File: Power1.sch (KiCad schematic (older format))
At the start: 88 parts, among them J2 XT60PW-M, Q4 BSS138W, Q5 SISS30DN-T1-GE3, Q6 SISS30DN-T1-GE3, U3 LMR33630BRNXR, U4 TPS2121RUXT, U5 BTS6143DAUMA1, U6 LTC3862EUH-1#PBF

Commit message: PVT
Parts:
- removed C15, C17, C20: 22u, Capacitor-Chip:C_CHIP_2012_Reflow, symbol passive:C
- removed C16: 100n, Capacitor-Chip:C_CHIP_1005_Hand_NoSilk, symbol passive:C
- removed R17: 1k, Resistor-Chip:R_CHIP_1005_Hand_NoSilk, symbol passive:R
- added C17: 47u, Phoenix:C_RADIAL_5.0_P2.0_D0.5, symbol passive:CE_Polarity
- added C19, C21, C22, C8: 10u, Capacitor-Chip:C_CHIP_2012_Reflow, symbol passive:C
- added C38, C40: 100n, Capacitor-Chip:C_CHIP_1608_Reflow, symbol passive:C
- C12: renamed from C10; PartName C1005X5R1V105K050BE -> TMK105BJ105MV-F
- C16: renamed from C14; PartName C1005X5R1V105K050BE -> TMK105BJ105MV-F
- C18: value 22u -> 10u; PartName GRM21BR61E226ME44L -> GRM21BC8YA106KE11L
- C20: renamed from C19; PartName UVZ1V331MPD -> 35ZLH330MEFCT810X12.5
- C25: renamed from C23; footprint Capacitor-Chip:C_CHIP_1608_Reflow -> Capacitor-Chip:C_CHIP_2012_Reflow; PartName EMK107BBJ106MA-T -> GRM21BC8YA106KE11L
- C28: renamed from C26; PartName UMK325BJ106MM-P -> GMK325BJ106KN-T
- C29: renamed from C27; footprint Capacitor-Chip:C_CHIP_1608_Reflow -> Capacitor-Chip:C_CHIP_1005_Hand_NoSilk; PartName GRM188R61E105KA12D -> TMK105BJ105MV-F
- C32: renamed from C30; PartName UMK325BJ106MM-P -> GMK325BJ106KN-T
- C33: renamed from C31; PartName UMK325BJ106MM-P -> GMK325BJ106KN-T
- C34: renamed from C33; value 33u -> 56u; PartName 63PZE33M8X9 -> 63SXE56M
- C35: renamed from C32; PartName UMK325BJ106MM-P -> GMK325BJ106KN-T
- C36: value 33u -> 56u; PartName 63PZE33M8X9 -> 63SXE56M
- C37: renamed from C34; PartName UMK325BJ106MM-P -> GMK325BJ106KN-T
- C39: renamed from C35; PartName UMK325BJ106MM-P -> GMK325BJ106KN-T
- C7: renamed from C6; footprint Capacitor-Chip:C_CHIP_3225_Reflow -> Capacitor-Chip:C_CHIP_2012_Reflow; PartName UMK325BJ106MM-P -> GRM21BC8YA106KE11L
- C9: renamed from C8; value 4.7u -> 10u; PartName (none) -> GRM21BC8YA106KE11L
- F1: value 30A -> 25A; PartName 0685H9300-01 -> 0685H9250-01
- R21: renamed from R22; value 68k -> 75k; PartName RK73H1ETTP6802F -> RK73H1ETTP7502F
- R22: renamed from R23; value 30k -> 43k; PartName RK73H1ETTP3002F -> RK73H1ETTP4302F
- R30: renamed from R31; value 5m -> 7m; PartName KRL6432E-M-R005-F-T1 -> KRL6432E-M-R007-F-T1
- R31: renamed from R32; value 5m -> 7m; PartName KRL6432E-M-R005-F-T1 -> KRL6432E-M-R007-F-T1
- U4: value TPS2121RUXT -> TPS2121RUXR; PartName TPS2121RUXT -> TPS2121RUXR
- renumbered C7 to C10, C9 to C11, C11 to C13, C12 to C14, C13 to C15, C21 to C23, C22 to C24, C24 to C26, C25 to C27, C28 to C30, C29 to C31, R14 to R13, R13 to R14, R20 to R17, R21 to R18, R18 to R19, R19 to R20, R24 to R23, R25 to R24, R26 to R25, R27 to R26, R28 to R27, R29 to R28, R30 to R29
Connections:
- net +12V: now also U4.7 (IN1), C19.1, C21.1, C22.1; no longer U4.2 (IN2)
- net +48V: now also C38.1, C40.1
- net GND: now also U4.3 (CP2), U4.5 (OV1), C17.2, C19.2, C21.2, C22.2, C38.2, C40.2, C8.2; no longer U4.4 (OV2), U4.6 (PR1)
- net VBAT: now also C8.1
- net VBUS: now also U4.2 (IN2); no longer U4.7 (IN1)
- net VSYS: now also C17.1
- net at U5.2 (IN): now also Q4.3 (D)
- net at R13.1, R15.2: now also U4.6 (PR1); no longer U4.3 (CP2)
- net at R12.1, R14.2: now also U4.4 (OV2); no longer U4.5 (OV1)
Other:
- note added: "VBAT to 48V/8A Boost Converter"
- note added: "old\nST=Z : IN1(VBUS) is selected\nST=L : IN2(12V) is selected"
- note removed: "ST=Z : IN1(VBUS) is selected\nST=L : IN2(12V) is selected"
- note removed: "VBAT to 48V/10A Boost Converter"
- moved on the sheet: C10, C11, C12, C15, C34, C36, C9, L1, R12, R13, R14, R15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

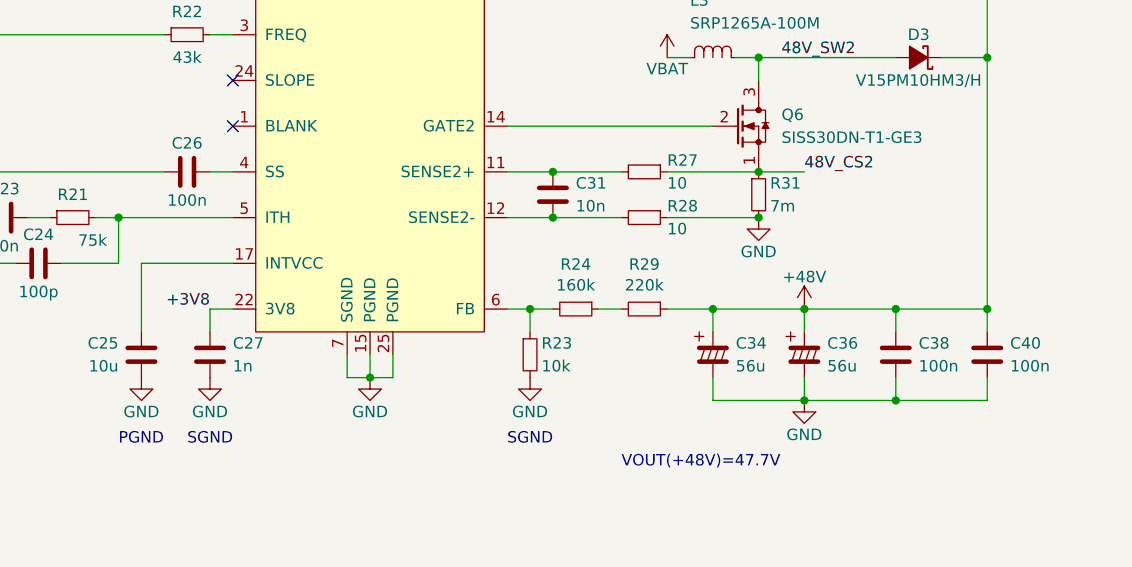
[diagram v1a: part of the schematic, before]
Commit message: SBUにTVSダイオードを追加
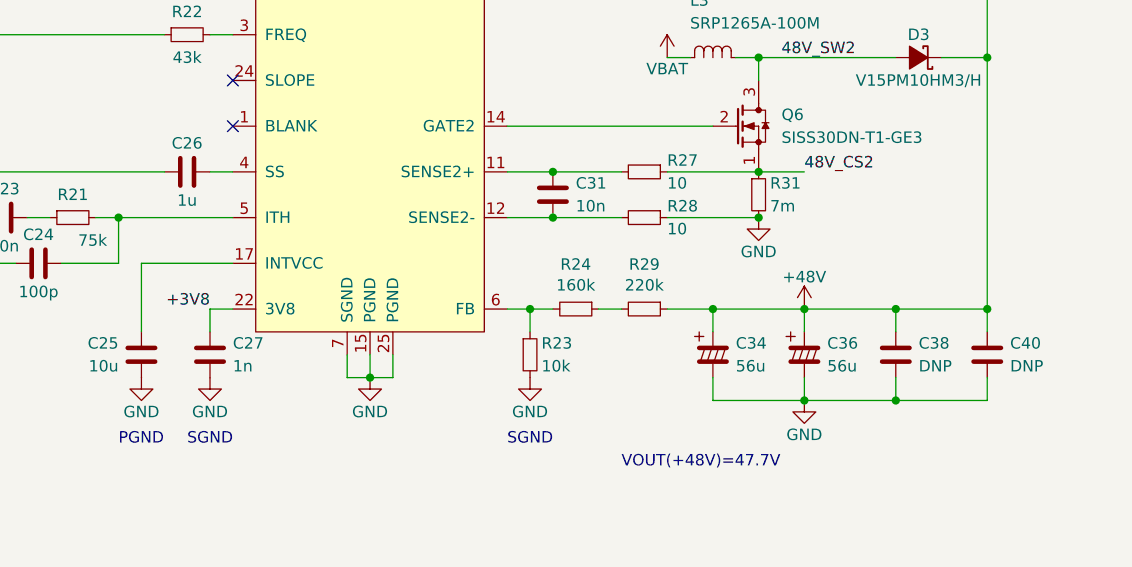
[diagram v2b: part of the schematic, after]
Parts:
- C26: value 100n -> 1u; PartName GRM155R71H104ME14D -> TMK105BJ105MV-F
- C38, C40: value 100n -> DNP; Supplier (none) -> None
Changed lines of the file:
@@
 P 7200 5100
 F 0 "C26" V 7075 5100 50  0000 C CNN
-F 1 "100n" V 7325 5100 50  0000 C CNN
+F 1 "1u" V 7325 5100 50  0000 C CNN
 F 2 "Capacitor-Chip:C_CHIP_1005_Hand_NoSilk" H 7300 5000 50  0001 C CNN
 F 3 "" H 7225 5200 50  0001 C CNN
-F 4 "GRM155R71H104ME14D" H 7200 5100 50  0001 C CNN "PartName"
+F 4 "TMK105BJ105MV-F" H 7200 5100 50  0001 C CNN "PartName"
 	1    7200 5100
 	0    -1   1    0
@@
 AR Path="/5E314B49/5FB00ABF" Ref="C38"  Part="1"
 F 0 "C38" H 10400 5950 50  0000 L CNN
-F 1 "100n" H 10400 5850 50  0000 L CNN
+F 1 "DNP" H 10400 5850 50  0000 L CNN
 F 2 "Capacitor-Chip:C_CHIP_1608_Reflow" H 10400 5800 50  0001 C CNN
 F 3 "" H 10325 6000 50  0001 C CNN
 F 4 "GCJ188R72A104KA01D" H 10300 5900 50  0001 C CNN "PartName"
+F 5 "None" H 10300 5900 50  0001 C CNN "Supplier"
 	1    10300 5900
 	1    0    0    -1
@@
 AR Path="/5E314B49/5FB0C188" Ref="C40"  Part="1"
 F 0 "C40" H 10800 5950 50  0000 L CNN
-F 1 "100n" H 10800 5850 50  0000 L CNN
+F 1 "DNP" H 10800 5850 50  0000 L CNN
 F 2 "Capacitor-Chip:C_CHIP_1608_Reflow" H 10800 5800 50  0001 C CNN
 F 3 "" H 10725 6000 50  0001 C CNN
 F 4 "GCJ188R72A104KA01D" H 10700 5900 50  0001 C CNN "PartName"
+F 5 "None" H 10700 5900 50  0001 C CNN "Supplier"
 	1    10700 5900
 	1    0    0    -1
